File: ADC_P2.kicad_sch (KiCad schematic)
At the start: 32 parts, among them U107 ADR4540, U111 ADA4841-1, U97 AD7768

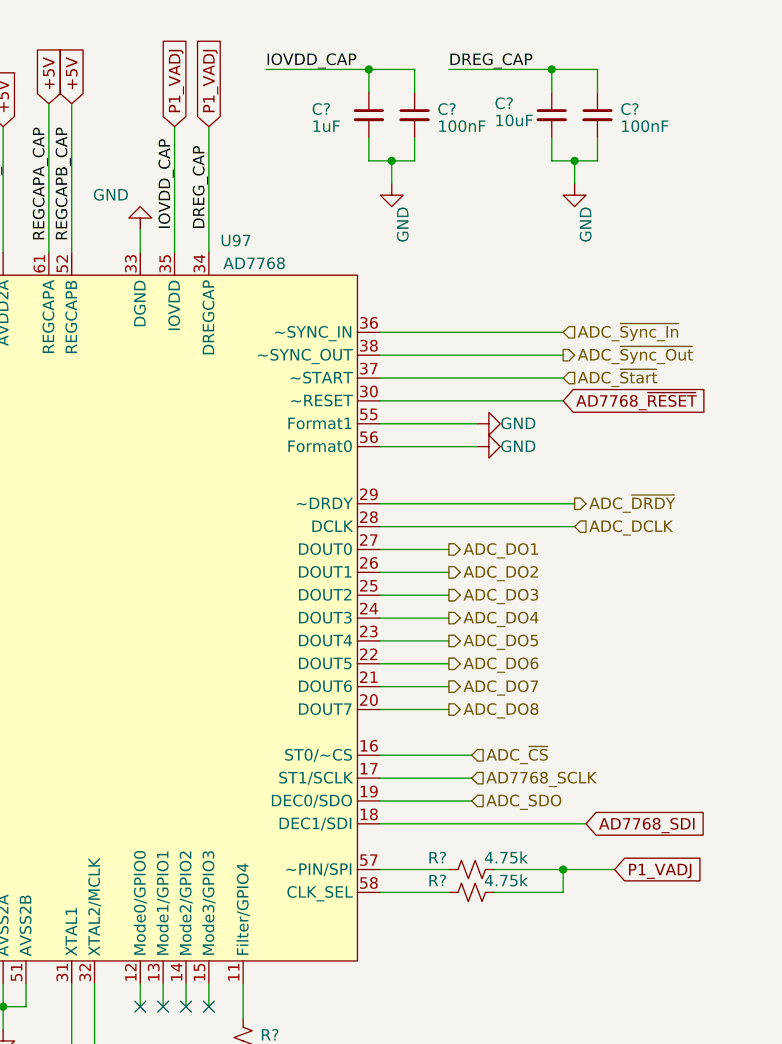
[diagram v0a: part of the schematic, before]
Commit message: Changed ADCs to run on +2.5V VADJ
Modified schematic to allow the ADCs to be run from the +2.5V VADJ inputs on the FMC connector.
-All relevant ERC issues ran been looked into.
-Still working on all Board DRC issues.
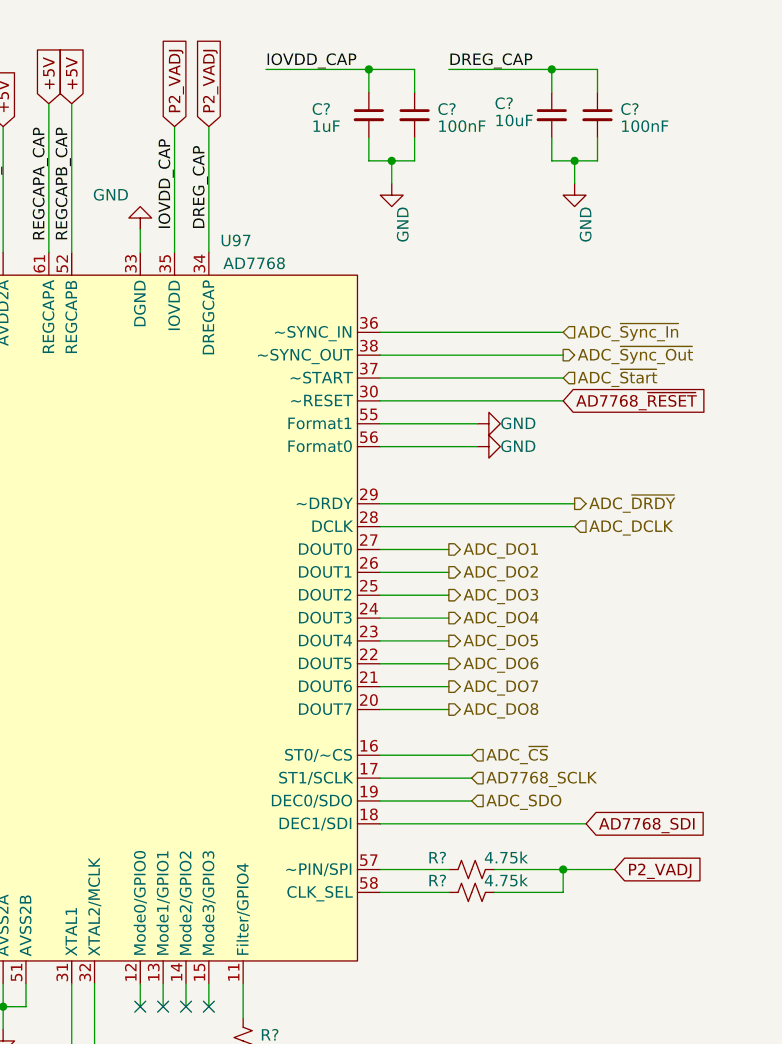
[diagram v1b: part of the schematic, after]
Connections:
- net P1_VADJ renamed P2_VADJ
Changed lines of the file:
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@@
+    )
+  )
+  (global_label "P2_VADJ" (shape input) (at 191.135 33.02 90) (fields_autoplaced)
+    (effects (font (size 1.27 1.27)) (justify left))
+    (property "Intersheetrefs" "${INTERSHEET_REFS}" (at 191.135 22.2523 90)
+      (effects (font (size 1.27 1.27)) (justify left) hide)
     )
   )
@@
     )
   )
-  (global_label "P1_VADJ" (shape input) (at 191.135 33.02 90) (fields_autoplaced)
+  (global_label "P2_VADJ" (shape input) (at 187.325 33.02 90) (fields_autoplaced)
     (effects (font (size 1.27 1.27)) (justify left))
-    (property "Intersheetrefs" "${INTERSHEET_REFS}" (at 191.135 22.2523 90)
+    (property "Intersheetrefs" "${INTERSHEET_REFS}" (at 187.325 22.2523 90)
       (effects (font (size 1.27 1.27)) (justify left) hide)
     )
@@
     )
   )
-  (global_label "P1_VADJ" (shape input) (at 236.22 115.57 0) (fields_autoplaced)
+  (global_label "P2_VADJ" (shape input) (at 236.22 115.57 0) (fields_autoplaced)
     (effects (font (size 1.27 1.27)) (justify left))
     (property "Intersheetrefs" "${INTERSHEET_REFS}" (at 246.9877 115.57 0)
       (effects (font (size 1.27 1.27)) (justify left) hide)
     )
-  )
-  (global_label "P1_VADJ" (shape input) (at 187.325 33.02 90) (fields_autoplaced)
-    (effects (font (size 1.27 1.27)) (justify left))
-    (property "Intersheetrefs" "${INTERSHEET_REFS}" (at 187.325 22.2523 90)
-      (effects (font (size 1.27 1.27)) (justify left) hide)
-    )
